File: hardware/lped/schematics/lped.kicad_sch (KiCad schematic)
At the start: 24 parts, among them J1 ~{RESET}, J2 SWDCLK, J3 SWDIO, J4 3V3, J5 DOCK_CONN, J7 GND, U1 nRF52833_QDxx, Y1 32MHz

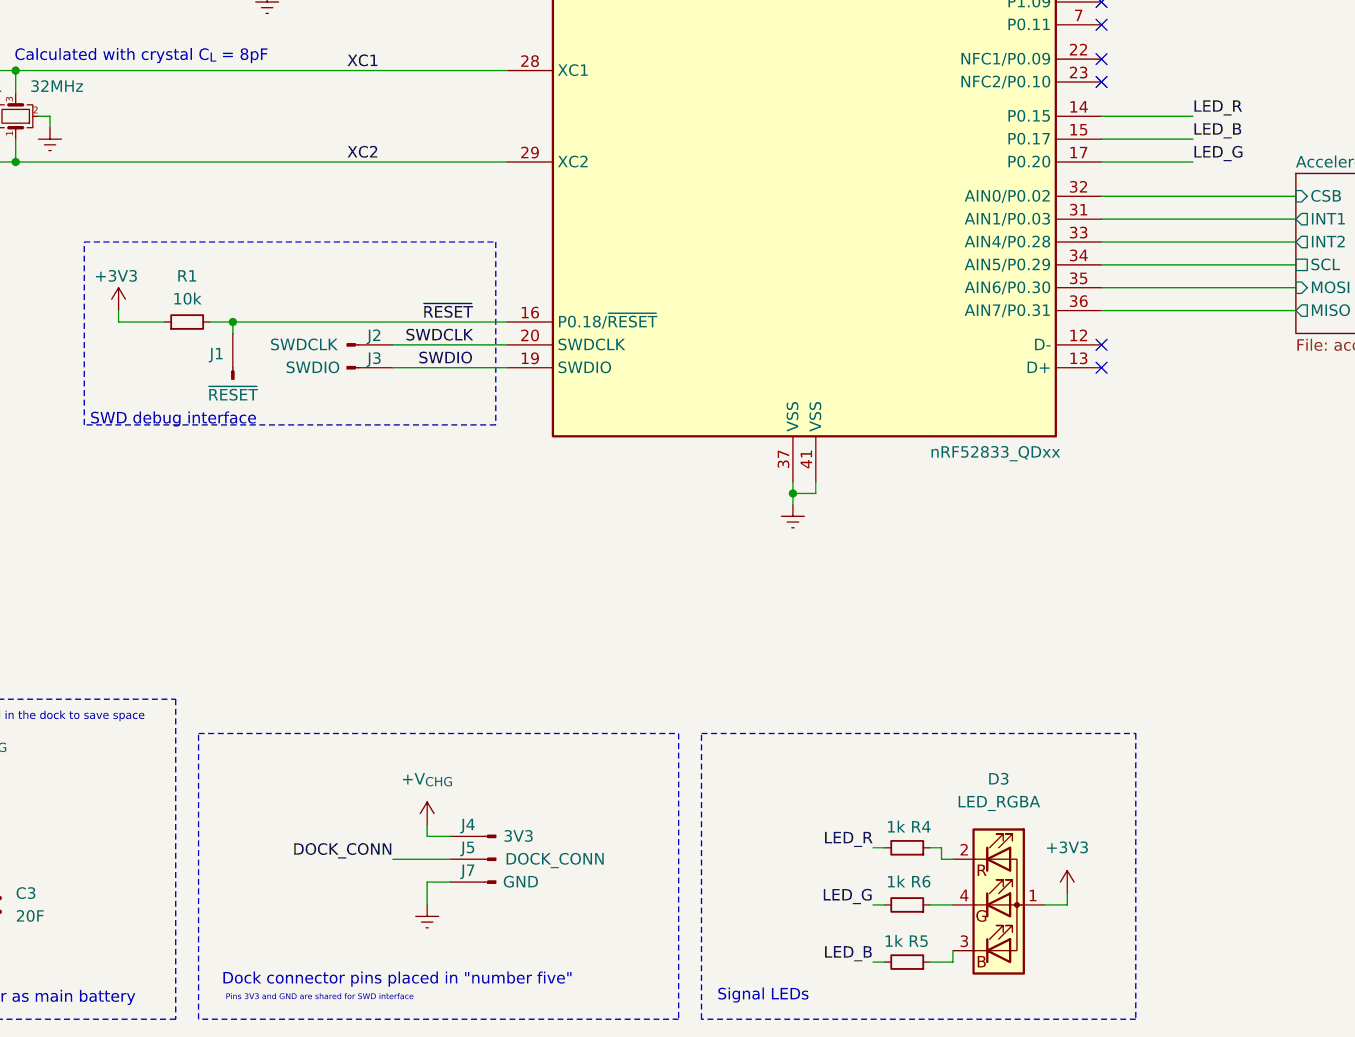
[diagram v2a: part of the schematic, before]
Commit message: fix(hardware): LPED PCB clean up
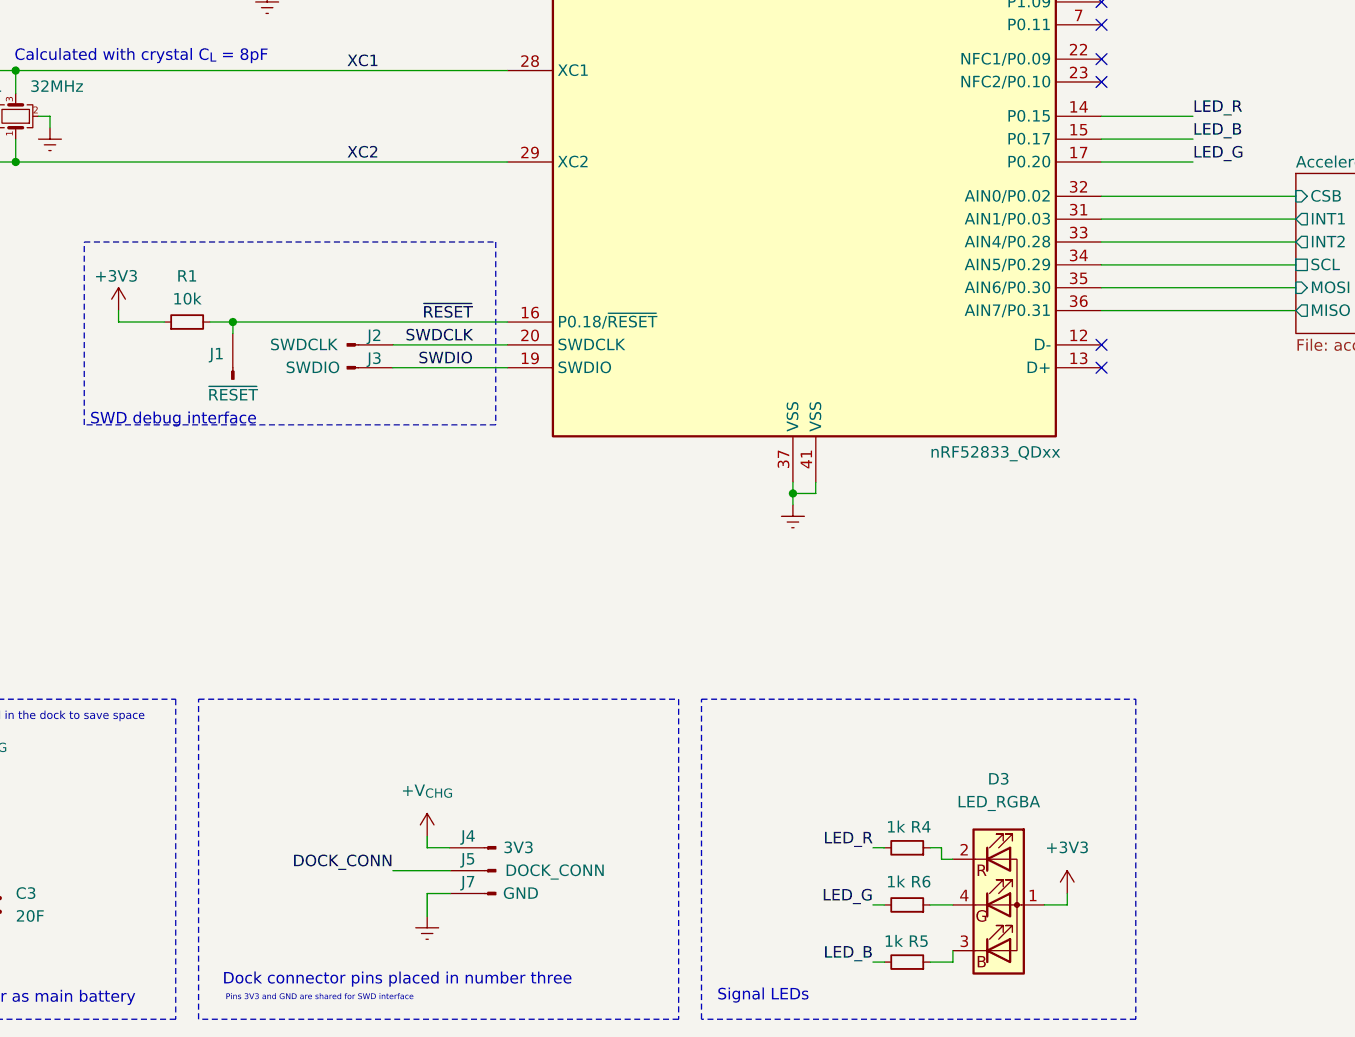
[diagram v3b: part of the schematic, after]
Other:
- note added: "Dock connector pins placed in number three"
- note removed: "Dock connector pins placed in "number five""
- moved on the sheet: J4, J5, J7
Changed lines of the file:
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@@
 	)
 	(rectangle
-		(start 60.96 163.83)
+		(start 60.96 160.02)
 		(end 114.3 195.58)
 		(stroke
@@
 	)
 	(rectangle
-		(start 116.84 163.83)
+		(start 116.84 160.02)
 		(end 165.1 195.58)
 		(stroke
@@
 		)
 	)
-	(text "Dock connector pins placed in \"number five\""
+	(text "Dock connector pins placed in number three"
 		(exclude_from_sim no)
 		(at 83.058 191.262 0)
@@
 	)
 	(no_connect
+		(at 161.29 120.65)
+	)
+	(no_connect
 		(at 161.29 80.01)
 	)
@@
 	)
 	(no_connect
-		(at 161.29 120.65)
-	)
-	(no_connect
 		(at 161.29 82.55)
 	)
@@
 	)
 	(no_connect
+		(at 161.29 88.9)
+	)
+	(no_connect
 		(at 161.29 123.19)
 	)
-	(no_connect
-		(at 161.29 88.9)
-	)
 	(wire
 		(pts
@@
 	(wire
 		(pts
-			(xy 86.36 175.26) (xy 86.36 173.99)
+			(xy 86.36 176.53) (xy 86.36 175.26)
 		)
 		(stroke
@@
 	(wire
 		(pts
-			(xy 86.36 180.34) (xy 88.9 180.34)
+			(xy 86.36 181.61) (xy 88.9 181.61)
 		)
 		(stroke
@@
 	(wire
 		(pts
-			(xy 86.36 182.88) (xy 86.36 180.34)
+			(xy 86.36 184.15) (xy 86.36 181.61)
 		)
 		(stroke
@@
 	(wire
 		(pts
-			(xy 88.9 175.26) (xy 86.36 175.26)
+			(xy 88.9 176.53) (xy 86.36 176.53)
 		)
 		(stroke
@@
 	(wire
 		(pts
-			(xy 82.55 177.8) (xy 88.9 177.8)
+			(xy 82.55 179.07) (xy 88.9 179.07)
 		)
 		(stroke
@@
 	(wire
 		(pts
-			(xy 171.45 100.33) (xy 161.29 100.33)
-		)
-		(stroke
-			(width 0)
-			(type default)
-		)
-	)
-	(wire
-		(pts
 			(xy 43.18 72.39) (xy 58.42 72.39)
 		)
@@
 	(wire
 		(pts
+			(xy 161.29 100.33) (xy 171.45 100.33)
+		)
+		(stroke
+			(width 0)
+			(type default)
+		)
+	)
+	(wire
+		(pts
 			(xy 143.51 177.8) (xy 144.78 177.8)
 		)
@@
 			(width 0)
 			(type default)
+		)
+	)
+	(label "DEC1"
+		(at 67.31 50.8 0)
+		(effects
+			(font
+				(size 1.27 1.27)
+			)
+			(justify left bottom)
+		)
+	)
+	(label "LED_B"
+		(at 171.45 97.79 0)
+		(effects
+			(font
+				(size 1.27 1.27)
+			)
+			(justify left bottom)
+		)
+	)
+	(label "XC1"
+		(at 77.47 90.17 0)
+		(effects
+			(font
+				(size 1.27 1.27)
+			)
+			(justify left bottom)
+		)
+	)
+	(label "ANT_FILT"
+		(at 44.45 72.39 0)
+		(effects
+			(font
+				(size 1.27 1.27)
+			)
+			(justify left bottom)
 		)
 	)
@@
 		)
 	)
-	(label "DEC1"
-		(at 67.31 50.8 0)
-		(effects
-			(font
-				(size 1.27 1.27)
-			)
-			(justify left bottom)
-		)
-	)
-	(label "LED_B"
-		(at 171.45 97.79 0)
-		(effects
-			(font
-				(size 1.27 1.27)
-			)
-			(justify left bottom)
-		)
-	)
-	(label "XC1"
-		(at 77.47 90.17 0)
-		(effects
-			(font
-				(size 1.27 1.27)
-			)
-			(justify left bottom)
-		)
-	)
-	(label "ANT_FILT"
-		(at 44.45 72.39 0)
-		(effects
-			(font
-				(size 1.27 1.27)
-			)
-			(justify left bottom)
-		)
-	)
 	(label "DOCK_CONN"
-		(at 82.55 177.8 180)
+		(at 82.55 179.07 180)
 		(effects
 			(font
@@
 	(symbol
 		(lib_id "power:+3V3")
-		(at 86.36 173.99 0)
+		(at 86.36 175.26 0)
 		(unit 1)
 		(exclude_from_sim no)
@@
 		(fields_autoplaced yes)
 		(property "Reference" "#PWR013"
-			(at 86.36 177.8 0)
+			(at 86.36 179.07 0)
 			(effects
 				(font
@@
 		)
 		(property "Value" "+V_{CHG}"
-			(at 86.36 168.91 0)
+			(at 86.36 170.18 0)
 			(effects
 				(font
@@
 		)
 		(property "Footprint" ""
-			(at 86.36 173.99 0)
+			(at 86.36 175.26 0)
 			(effects
 				(font
@@
 		)
 		(property "Datasheet" ""
-			(at 86.36 173.99 0)
+			(at 86.36 175.26 0)
 			(effects
 				(font
@@
 		)
 		(property "Description" "Power symbol creates a global label with name \"+3V3\""
-			(at 86.36 173.99 0)
+			(at 86.36 175.26 0)
 			(effects
 				(font
@@
 	(symbol
 		(lib_id "Connector:Conn_01x01_Pin")
-		(at 93.98 175.26 180)
+		(at 93.98 176.53 180)
 		(unit 1)
 		(exclude_from_sim no)
@@
 		(dnp no)
 		(property "Reference" "J4"
-			(at 90.932 173.99 0)
+			(at 90.932 175.26 0)
 			(effects
 				(font
@@
 		)
 		(property "Value" "3V3"
-			(at 96.52 175.26 0)
+			(at 96.52 176.53 0)
 			(effects
 				(font
@@
 		)
 		(property "Footprint" "TestPoint:TestPoint_Pad_D2.0mm"
-			(at 93.98 175.26 0)
+			(at 93.98 176.53 0)
 			(effects
 				(font
@@
 		)
 		(property "Datasheet" "~"
-			(at 93.98 175.26 0)
+			(at 93.98 176.53 0)
 			(effects
 				(font
@@
 		)
 		(property "Description" "Generic connector, single row, 01x01, script generated"
-			(at 93.98 175.26 0)
+			(at 93.98 176.53 0)
 			(effects
 				(font
@@
 	(symbol
 		(lib_id "Connector:Conn_01x01_Pin")
-		(at 93.98 180.34 180)
+		(at 93.98 181.61 180)
 		(unit 1)
 		(exclude_from_sim no)
@@
 		(dnp no)
 		(property "Reference" "J7"
-			(at 90.932 179.07 0)
+			(at 90.932 180.34 0)
 			(effects
 				(font
@@
 		)
 		(property "Value" "GND"
-			(at 96.774 180.34 0)
+			(at 96.774 181.61 0)
 			(effects
 				(font
@@
 		)
 		(property "Footprint" "TestPoint:TestPoint_Pad_2.0x2.0mm"
-			(at 93.98 180.34 0)
+			(at 93.98 181.61 0)
 			(effects
 				(font
@@
 		)
 		(property "Datasheet" "~"
-			(at 93.98 180.34 0)
+			(at 93.98 181.61 0)
 			(effects
 				(font
@@
 		)
 		(property "Description" "Generic connector, single row, 01x01, script generated"
-			(at 93.98 180.34 0)
+			(at 93.98 181.61 0)
 			(effects
 				(font
@@
 	(symbol
 		(lib_id "Connector:Conn_01x01_Pin")
-		(at 93.98 177.8 180)
+		(at 93.98 179.07 180)
 		(unit 1)
 		(exclude_from_sim no)
@@
 		(dnp no)
 		(property "Reference" "J5"
-			(at 90.932 176.53 0)
+			(at 90.932 177.8 0)
 			(effects
 				(font
@@
 		)
 		(property "Value" "DOCK_CONN"
-			(at 100.584 177.8 0)
+			(at 100.584 179.07 0)
 			(effects
 				(font
@@
 		)
 		(property "Footprint" "TestPoint:TestPoint_Pad_D2.0mm"
-			(at 93.98 177.8 0)
+			(at 93.98 179.07 0)
 			(effects
 				(font
@@
 		)
 		(property "Datasheet" "~"
-			(at 93.98 177.8 0)
+			(at 93.98 179.07 0)
 			(effects
 				(font
@@
 		)
 		(property "Description" "Generic connector, single row, 01x01, script generated"
-			(at 93.98 177.8 0)
+			(at 93.98 179.07 0)
 			(effects
 				(font
@@
 	(symbol
 		(lib_id "power:Earth")
-		(at 86.36 182.88 0)
+		(at 86.36 184.15 0)
 		(unit 1)
 		(exclude_from_sim no)
@@
 		(fields_autoplaced yes)
 		(property "Reference" "#PWR014"
+			(at 86.36 190.5 0)
+			(effects
+				(font
+					(size 1.27 1.27)
+				)
+				(hide yes)
+			)
+		)
+		(property "Value" "Earth"
 			(at 86.36 189.23 0)
 			(effects
@@
 			)
 		)
-		(property "Value" "Earth"
-			(at 86.36 187.96 0)
-			(effects
-				(font
-					(size 1.27 1.27)
-				)
-				(hide yes)
-			)
-		)
 		(property "Footprint" ""
-			(at 86.36 182.88 0)
+			(at 86.36 184.15 0)
 			(effects
 				(font
@@
 		)
 		(property "Datasheet" "~"
-			(at 86.36 182.88 0)
+			(at 86.36 184.15 0)
 			(effects
 				(font
@@
 		)
 		(property "Description" "Power symbol creates a global label with name \"Earth\""
-			(at 86.36 182.88 0)
-			(effects
-				(font
+			(at 86.36 184.15 0)
+			(effects
+				(font
